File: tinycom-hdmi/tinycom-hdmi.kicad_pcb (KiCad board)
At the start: 2 copper layers, 45.2 x 45.2 mm, 77 parts, among them J1 MICRO_SD_HINGE, P1 CONN_02X10, P2 CONN_02X10, P4 USB_OTG, U1 SY8008BAAC, U2 AXP209, U3 SY8008BAAC, U4 RTL8188, U5 rainsun-antenna, U6 RCLAMP0524P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

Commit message: readme
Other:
- net class Default: trace_width 0.2 -> 2
- board text added: "rev. 1"
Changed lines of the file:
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@@
     (links 247)
     (no_connects 0)
-    (area 124.384999 79.172999 169.747001 124.535001)
+    (area 114.725715 73.970334 181.402285 124.535001)
     (thickness 1.6)
-    (drawings 14)
+    (drawings 15)
     (tracks 925)
     (zones 0)
@@
   )
   (setup
-    (last_trace_width 0.2)
+    (last_trace_width 2)
     (trace_clearance 0.14)
     (zone_clearance 0.2)
@@
   (net_class Default "This is the default net class."
     (clearance 0.14)
-    (trace_width 0.2)
+    (trace_width 2)
     (via_dia 0.6)
     (via_drill 0.3)
@@
     )
   )
+  (gr_text "rev. 1" (at 167.897 101.982 90) (layer B.SilkS)
+    (effects (font (size 0.8 0.8) (thickness 0.1)) (justify mirror))
+  )
   (gr_text http://tinycom.org/ (at 158.115 102.108 90) (layer B.SilkS)
     (effects (font (size 1 1) (thickness 0.15)) (justify mirror))
@@
   (segment (start 158.782 105.872) (end 159.292 106.382) (width 0.2) (layer F.Cu) (net 69))
   (segment (start 159.292 106.382) (end 160.185 106.382) (width 0.2) (layer F.Cu) (net 69))
-  (segment (start 154.697 112.442) (end 155.377 112.442) (width 0.4) (layer F.Cu) (net 70))
-  (segment (start 155.377 112.442) (end 155.387 112.452) (width 0.4) (layer F.Cu) (net 70))
-  (segment (start 152.527 111.652) (end 153.907 111.652) (width 0.4) (layer F.Cu) (net 70))
-  (segment (start 153.907 111.652) (end 154.697 112.442) (width 0.4) (layer F.Cu) (net 70))
+  (segment (start 154.697 112.442) (end 155.377 112.442) (width 0.6) (layer F.Cu) (net 70))
+  (segment (start 155.377 112.442) (end 155.387 112.452) (width 0.6) (layer F.Cu) (net 70))
+  (segment (start 153.907 111.652) (end 154.697 112.442) (width 0.6) (layer F.Cu) (net 70))
+  (segment (start 152.527 111.652) (end 153.907 111.652) (width 0.6) (layer F.Cu) (net 70))
   (segment (start 152.527 111.652) (end 152.8 111.652) (width 0.4) (layer F.Cu) (net 70))
   (segment (start 152.273 111.652) (end 152.292 111.652) (width 0.4) (layer F.Cu) (net 70))
-  (segment (start 159.207 113.284) (end 158.383 112.46) (width 0.4) (layer F.Cu) (net 71))
-  (segment (start 158.383 112.46) (end 157.179 112.46) (width 0.4) (layer F.Cu) (net 71))
+  (segment (start 157.177 112.462) (end 158.385 112.462) (width 0.6) (layer F.Cu) (net 71))
+  (segment (start 158.385 112.462) (end 159.207 113.284) (width 0.6) (layer F.Cu) (net 71))
+  (segment (start 156.487 112.452) (end 157.167 112.452) (width 0.6) (layer F.Cu) (net 71))
+  (segment (start 157.167 112.452) (end 157.177 112.462) (width 0.6) (layer F.Cu) (net 71))
   (segment (start 157.179 112.46) (end 157.177 112.462) (width 0.4) (layer F.Cu) (net 71))
-  (segment (start 156.487 112.452) (end 157.167 112.452) (width 0.4) (layer F.Cu) (net 71))
-  (segment (start 157.167 112.452) (end 157.177 112.462) (width 0.4) (layer F.Cu) (net 71))
   (segment (start 158.877 112.522) (end 159.237 112.522) (width 0.4) (layer F.Cu) (net 71))
   (segment (start 153.63 95.91) (end 153.02 96.52) (width 0.2) (layer F.Cu) (net 74))

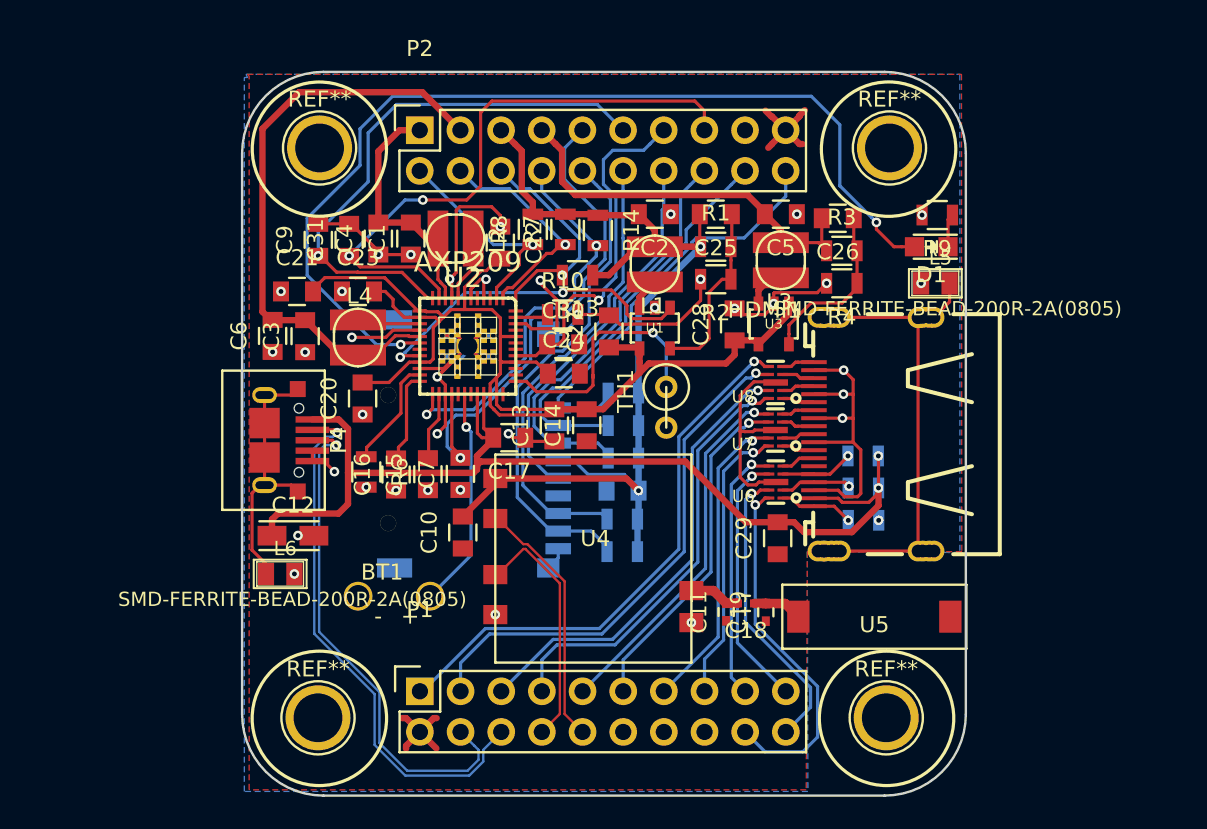
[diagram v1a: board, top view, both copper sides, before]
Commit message: add mic to hdmi
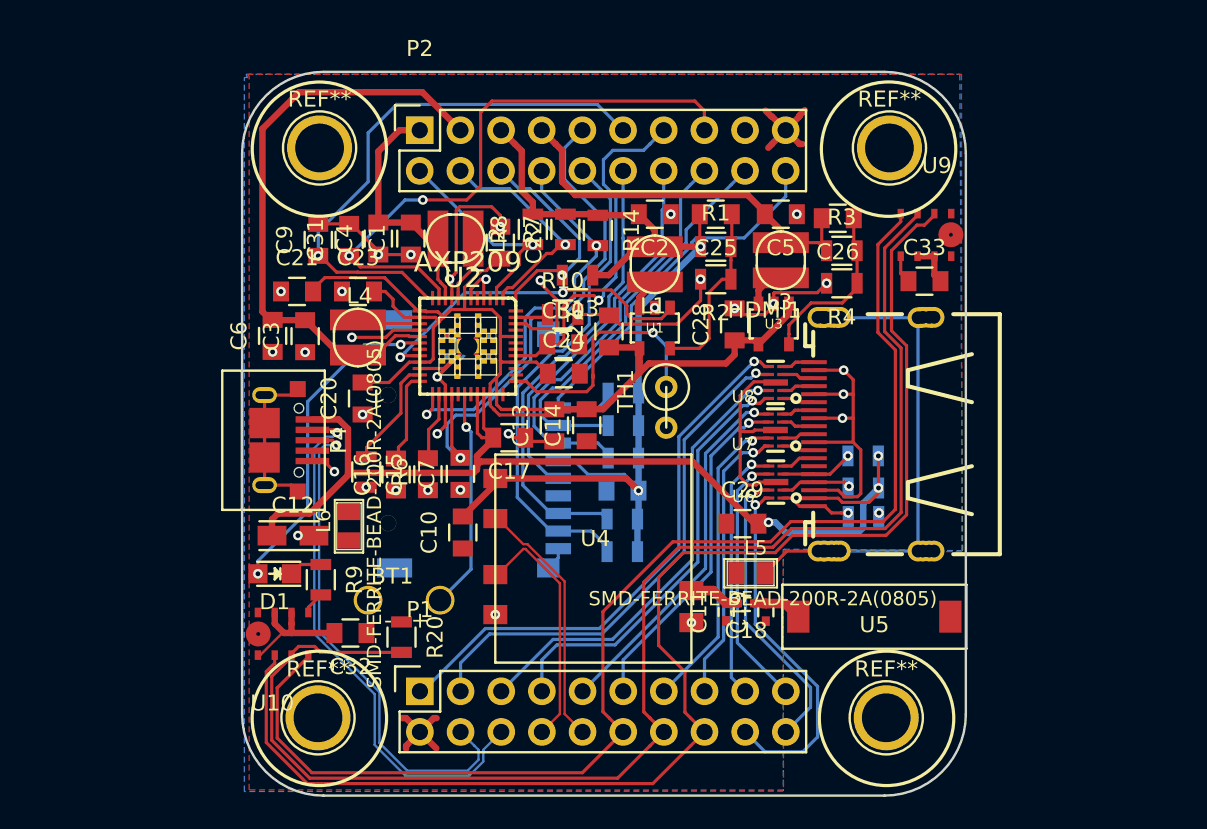
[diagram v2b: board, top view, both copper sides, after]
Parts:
- added C32: 10uF, Capacitors_SMD:C_0805, F.Cu at (131.2, 114.3)
- added C33: 10uF, Capacitors_SMD:C_0805, F.Cu at (167.1, 92.3)
- added R20: 100K, Resistors_SMD:R_0805, F.Cu at (134.4, 114.6)
- added U10: admp411, tinycom:admp411, F.Cu at (126.8, 114.4)
- added U9: admp411, tinycom:admp411, F.Cu at (167.4, 89.4)
- moved D1 45.8 mm to (126.5, 110.6)
- moved R9 44.7 mm to (129.4, 111.0), turned to 270 degrees
- moved L5 21.5 mm to (156.2, 110.6)
- moved L6 5.23 mm to (131.1, 107.6), turned to 90 degrees
- moved C29 2.38 mm to (155.7, 107.5), turned to 0 degrees
- moved BT1 0.67 mm to (134.6, 112.3)
- moved R12 0.24 mm to (163.3, 107.0)
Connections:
- P1 pad 12: Net-(P1-Pad12) -> I2S_SCK
- P1 pad 14: Net-(P1-Pad14) -> I2S_SD
- P1 pad 16: Net-(P1-Pad16) -> I2S_WS
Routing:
- net I2S_SD: track 0.00 -> 87.5 mm
- net I2S_WS: track 0.00 -> 84.0 mm
- net I2S_SCK: track 0.00 -> 78.0 mm
- net Net-(D1-Pad2): track 61.2 -> 20.6 mm
- net VCC_33: track 63.7 -> 74.6 mm
- net Net-(L6-Pad1): track 16.5 -> 10.4 mm
- net GND: track 131.7 -> 134.9 mm, vias 38 -> 35
- net Net-(HDMI1-PadSH1): track 27.1 -> 28.2 mm
- net +5V: track 66.1 -> 65.4 mm, vias 2 -> 3
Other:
- net class Default: trace_width 2 -> 0.2

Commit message: routing
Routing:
- net I2S_SCK: track 78.0 -> 74.5 mm
- net I2S_SD: track 87.5 -> 84.7 mm
- net VCC_12_INT: track 37.2 -> 35.2 mm
- net I2S_WS: track 84.0 -> 82.3 mm
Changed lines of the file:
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@@
   (general
     (links 273)
-    (no_connects 21)
-    (area 124.384999 79.172999 169.747001 124.535001)
+    (no_connects 9)
+    (area 116.007334 73.970334 173.806666 124.535001)
     (thickness 1.6)
     (drawings 15)
-    (tracks 1002)
+    (tracks 1016)
     (zones 0)
     (modules 82)
@@
   (segment (start 135.55726 94.98076) (end 131.93776 94.98076) (width 0.2) (layer F.Cu) (net 17))
   (segment (start 131.93776 94.98076) (end 131.699 94.742) (width 0.2) (layer F.Cu) (net 17))
+  (segment (start 126.365 94.742) (end 126.24 94.742) (width 0.4) (layer F.Cu) (net 18))
+  (segment (start 126.24 94.742) (end 125.73 94.232) (width 0.4) (layer F.Cu) (net 18))
+  (segment (start 125.73 94.232) (end 125.73 88.952) (width 0.4) (layer F.Cu) (net 18))
+  (segment (start 125.73 88.952) (end 125.818 88.952) (width 0.4) (layer F.Cu) (net 18))
+  (segment (start 132.21 82.395) (end 133.305 81.3) (width 0.4) (layer F.Cu) (net 18))
+  (segment (start 133.305 81.3) (end 136.505 81.3) (width 0.4) (layer F.Cu) (net 18))
+  (segment (start 125.818 88.952) (end 127.6 87.17) (width 0.4) (layer F.Cu) (net 18))
+  (segment (start 136.505 81.3) (end 138.097 82.892) (width 0.4) (layer F.Cu) (net 18))
+  (segment (start 127.6 87.17) (end 131.21 87.17) (width 0.4) (layer F.Cu) (net 18))
+  (segment (start 131.21 87.17) (end 132.21 86.17) (width 0.4) (layer F.Cu) (net 18))
+  (segment (start 132.21 86.17) (end 132.21 82.395) (width 0.4) (layer F.Cu) (net 18))
   (segment (start 134.035901 95.732091) (end 134.858911 95.732091) (width 0.2) (layer F.Cu) (net 18))
   (segment (start 132.825992 96.942) (end 134.035901 95.732091) (width 0.2) (layer F.Cu) (net 18))
@@
   (segment (start 134.90768 95.78086) (end 135.55726 95.78086) (width 0.2) (layer F.Cu) (net 18))
   (segment (start 134.858911 95.732091) (end 134.90768 95.78086) (width 0.2) (layer F.Cu) (net 18))
-  (segment (start 126.365 94.742) (end 126.24 94.742) (width 0.4) (layer F.Cu) (net 18))
-  (segment (start 125.73 94.232) (end 125.73 82.804) (width 0.4) (layer F.Cu) (net 18))
-  (segment (start 126.24 94.742) (end 125.73 94.232) (width 0.4) (layer F.Cu) (net 18))
-  (segment (start 125.73 82.804) (end 128.016 80.518) (width 0.4) (layer F.Cu) (net 18))
-  (segment (start 128.016 80.518) (end 135.723 80.518) (width 0.4) (layer F.Cu) (net 18))
-  (segment (start 135.723 80.518) (end 138.097 82.892) (width 0.4) (layer F.Cu) (net 18))
   (segment (start 128.397 94.758) (end 126.381 94.758) (width 0.4) (layer F.Cu) (net 18))
   (segment (start 126.381 94.758) (end 126.365 94.742) (width 0.4) (layer F.Cu) (net 18))
@@
   (segment (start 153.337 82.892) (end 153.337 81.670686) (width 0.2) (layer F.Cu) (net 82))
   (segment (start 153.337 81.670686) (end 152.736314 81.07) (width 0.2) (layer F.Cu) (net 82))
+  (segment (start 129.694979 116.379979) (end 129.827 116.379979) (width 0.2) (layer F.Cu) (net 84))
+  (segment (start 129.827 116.379979) (end 130.751675 116.379979) (width 0.2) (layer F.Cu) (net 84))
+  (segment (start 128.597 115.682) (end 128.597 116.182) (width 0.2) (layer F.Cu) (net 84))
+  (segment (start 128.597 116.182) (end 128.794979 116.379979) (width 0.2) (layer F.Cu) (net 84))
+  (segment (start 128.794979 116.379979) (end 129.827 116.379979) (width 0.2) (layer F.Cu) (net 84))
+  (segment (start 134.207 123.03) (end 145.719 123.03) (width 0.2) (layer F.Cu) (net 84))
+  (segment (start 133.250011 122.073011) (end 134.207 123.03) (width 0.2) (layer F.Cu) (net 84))
+  (segment (start 133.250011 118.878315) (end 133.250011 122.073011) (width 0.2) (layer F.Cu) (net 84))
+  (segment (start 130.751675 116.379979) (end 133.250011 118.878315) (width 0.2) (layer F.Cu) (net 84))
+  (segment (start 145.719 123.03) (end 147.403401 121.345599) (width 0.2) (layer F.Cu) (net 84))
+  (segment (start 147.403401 121.345599) (end 148.267 120.482) (width 0.2) (layer F.Cu) (net 84))
   (segment (start 165.607 88.102) (end 165.607 88.602) (width 0.2) (layer F.Cu) (net 84))
   (segment (start 165.607 88.602) (end 164.18 90.029) (width 0.2) (layer F.Cu) (net 84))
@@
   (segment (start 158.74 107.34) (end 157.476523 108.603477) (width 0.2) (layer F.Cu) (net 84))
   (segment (start 157.476523 108.603477) (end 151.366523 108.603477) (width 0.2) (layer F.Cu) (net 84))
-  (segment (start 128.82 123.03) (end 145.719 123.03) (width 0.2) (layer F.Cu) (net 84))
-  (segment (start 145.719 123.03) (end 148.267 120.482) (width 0.2) (layer F.Cu) (net 84))
-  (segment (start 126.65 120.86) (end 128.82 123.03) (width 0.2) (layer F.Cu) (net 84))
-  (segment (start 126.65 117.729) (end 126.65 120.86) (width 0.2) (layer F.Cu) (net 84))
-  (segment (start 128.597 115.682) (end 128.597 115.782) (width 0.2) (layer F.Cu) (net 84))
-  (segment (start 128.597 115.782) (end 126.65 117.729) (width 0.2) (layer F.Cu) (net 84))
+  (segment (start 133.917 123.370011) (end 147.918989 123.370011) (width 0.2) (layer F.Cu) (net 85))
+  (segment (start 130.610837 116.719989) (end 132.91 119.019152) (width 0.2) (layer F.Cu) (net 85))
+  (segment (start 132.91 122.363011) (end 133.917 123.370011) (width 0.2) (layer F.Cu) (net 85))
+  (segment (start 128.484989 116.719989) (end 130.610837 116.719989) (width 0.2) (layer F.Cu) (net 85))
+  (segment (start 127.547 115.682) (end 127.547 115.782) (width 0.2) (layer F.Cu) (net 85))
+  (segment (start 127.547 115.782) (end 128.484989 116.719989) (width 0.2) (layer F.Cu) (net 85))
+  (segment (start 132.91 119.019152) (end 132.91 122.363011) (width 0.2) (layer F.Cu) (net 85))
+  (segment (start 149.943401 121.345599) (end 150.807 120.482) (width 0.2) (layer F.Cu) (net 85))
+  (segment (start 147.918989 123.370011) (end 149.943401 121.345599) (width 0.2) (layer F.Cu) (net 85))
+  (segment (start 129.359002 115.512) (end 128.989001 115.141999) (width 0.2) (layer F.Cu) (net 85))
+  (segment (start 128.989001 115.141999) (end 127.987001 115.141999) (width 0.2) (layer F.Cu) (net 85))
+  (segment (start 134.417 115.512) (end 129.359002 115.512) (width 0.2) (layer F.Cu) (net 85))
+  (segment (start 127.987001 115.141999) (end 127.547 115.582) (width 0.2) (layer F.Cu) (net 85))
+  (segment (start 127.547 115.582) (end 127.547 115.682) (width 0.2) (layer F.Cu) (net 85))
   (segment (start 149.943401 119.618401) (end 150.807 120.482) (width 0.2) (layer F.Cu) (net 85))
   (segment (start 149.55 111.13) (end 149.55 119.225) (width 0.2) (layer F.Cu) (net 85))
@@
   (segment (start 151.736512 108.943488) (end 149.55 111.13) (width 0.2) (layer F.Cu) (net 85))
   (segment (start 157.61736 108.943488) (end 151.736512 108.943488) (width 0.2) (layer F.Cu) (net 85))
-  (segment (start 127.547 115.682) (end 127.547 115.782) (width 0.2) (layer F.Cu) (net 85))
-  (segment (start 127.547 115.782) (end 126.30999 117.01901) (width 0.2) (layer F.Cu) (net 85))
-  (segment (start 126.30999 117.01901) (end 126.30999 121.000838) (width 0.2) (layer F.Cu) (net 85))
-  (segment (start 126.30999 121.000838) (end 128.679163 123.370011) (width 0.2) (layer F.Cu) (net 85))
-  (segment (start 128.679163 123.370011) (end 147.918989 123.370011) (width 0.2) (layer F.Cu) (net 85))
-  (segment (start 147.918989 123.370011) (end 149.943401 121.345599) (width 0.2) (layer F.Cu) (net 85))
-  (segment (start 149.943401 121.345599) (end 150.807 120.482) (width 0.2) (layer F.Cu) (net 85))
-  (segment (start 134.417 115.512) (end 129.359002 115.512) (width 0.2) (layer F.Cu) (net 85))
-  (segment (start 129.359002 115.512) (end 128.989001 115.141999) (width 0.2) (layer F.Cu) (net 85))
-  (segment (start 128.989001 115.141999) (end 127.987001 115.141999) (width 0.2) (layer F.Cu) (net 85))
-  (segment (start 127.987001 115.141999) (end 127.547 115.582) (width 0.2) (layer F.Cu) (net 85))
-  (segment (start 127.547 115.582) (end 127.547 115.682) (width 0.2) (layer F.Cu) (net 85))
+  (segment (start 126.497 115.682) (end 126.497 116.182) (width 0.2) (layer F.Cu) (net 86))
+  (segment (start 126.497 116.182) (end 127.375 117.06) (width 0.2) (layer F.Cu) (net 86))
+  (segment (start 127.375 117.06) (end 130.37 117.06) (width 0.2) (layer F.Cu) (net 86))
+  (segment (start 130.37 117.06) (end 132.52 119.21) (width 0.2) (layer F.Cu) (net 86))
+  (segment (start 132.52 119.21) (end 132.52 122.53) (width 0.2) (layer F.Cu) (net 86))
+  (segment (start 132.52 122.53) (end 133.700021 123.710021) (width 0.2) (layer F.Cu) (net 86))
+  (segment (start 133.700021 123.710021) (end 150.118979 123.710021) (width 0.2) (layer F.Cu) (net 86))
+  (segment (start 150.118979 123.710021) (end 152.483401 121.345599) (width 0.2) (layer F.Cu) (net 86))
+  (segment (start 152.483401 121.345599) (end 153.347 120.482) (width 0.2) (layer F.Cu) (net 86))
   (segment (start 152.483401 119.618401) (end 153.347 120.482) (width 0.2) (layer F.Cu) (net 86))
   (segment (start 152.12 119.255) (end 152.483401 119.618401) (width 0.2) (layer F.Cu) (net 86))
@@
   (segment (start 150.48 110.822) (end 150.48 115.08) (width 0.2) (layer F.Cu) (net 86))
   (segment (start 167.707 88.102) (end 167.707 88.202) (width 0.2) (layer F.Cu) (net 86))
-  (segment (start 126.497 115.682) (end 126.497 116.182) (width 0.2) (layer F.Cu) (net 86))
-  (segment (start 125.96998 121.141676) (end 128.538327 123.710021) (width 0.2) (layer F.Cu) (net 86))
-  (segment (start 150.118979 123.710021) (end 152.483401 121.345599) (width 0.2) (layer F.Cu) (net 86))
-  (segment (start 126.497 116.182) (end 125.96998 116.70902) (width 0.2) (layer F.Cu) (net 86))
-  (segment (start 125.96998 116.70902) (end 125.96998 121.141676) (width 0.2) (layer F.Cu) (net 86))
-  (segment (start 128.538327 123.710021) (end 150.118979 123.710021) (width 0.2) (layer F.Cu) (net 86))
-  (segment (start 152.483401 121.345599) (end 153.347 120.482) (width 0.2) (layer F.Cu) (net 86))
   (zone (net 2) (net_name GND) (layer F.Cu) (hatch edge 0.508)
     (connect_pads (clearance 0.2))
